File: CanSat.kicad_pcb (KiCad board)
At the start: 2 copper layers, 55.6 x 55.5 mm, 78 parts, among them IC1 W25Q128JVPIQ, J1 USB_C_Receptacle, J2 Conn_Coaxial, M1 SG-90, M2 MountingHole_2.2mm_M2, SW1 SW_Push, SW2 SW_Push, U1 MPU-6050, U4 RFM98W-433S2, U5 RP2350_60QFN, U6 LM1085-5.0, U7 LM1085-3.3, U8 BMP280, U9 APS6404L-3SQR-ZR, Y2 ASE-12.000MHz-E-T

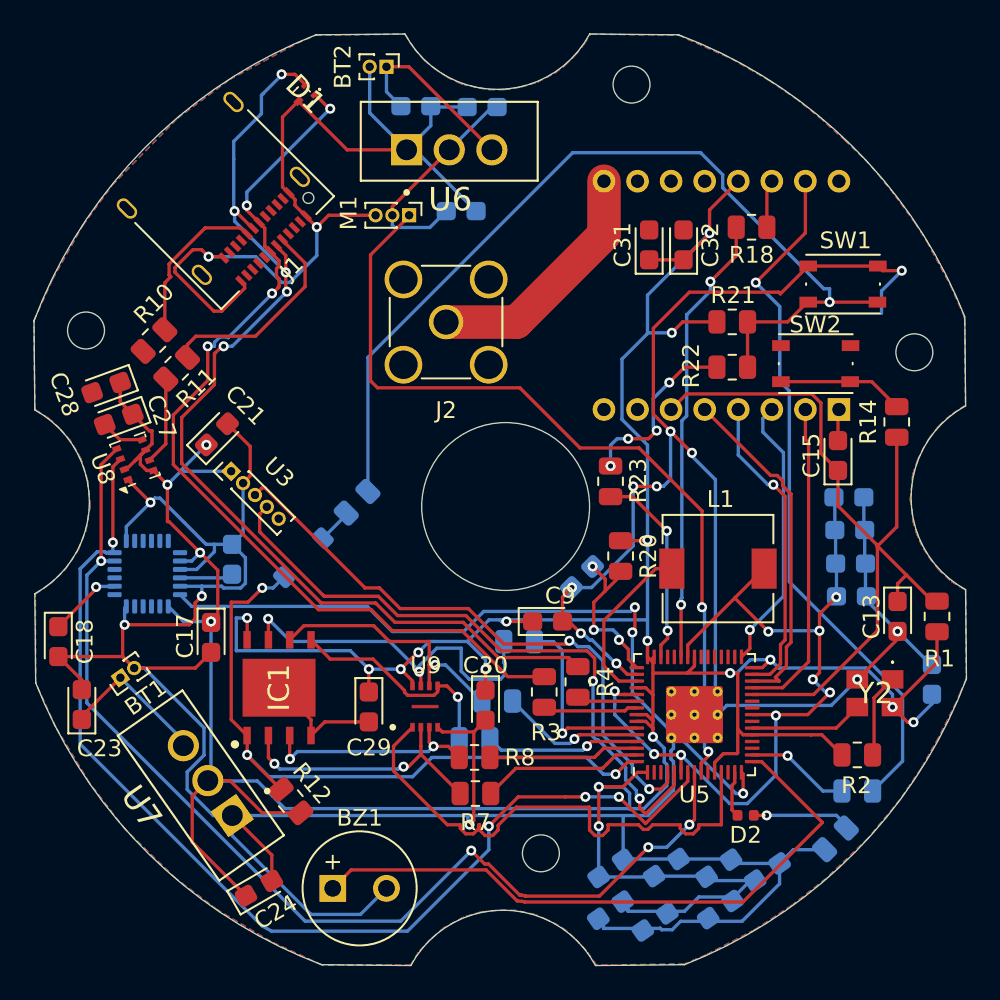
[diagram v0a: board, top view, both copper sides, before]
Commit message: Added pin headers, debug headers, changed power source
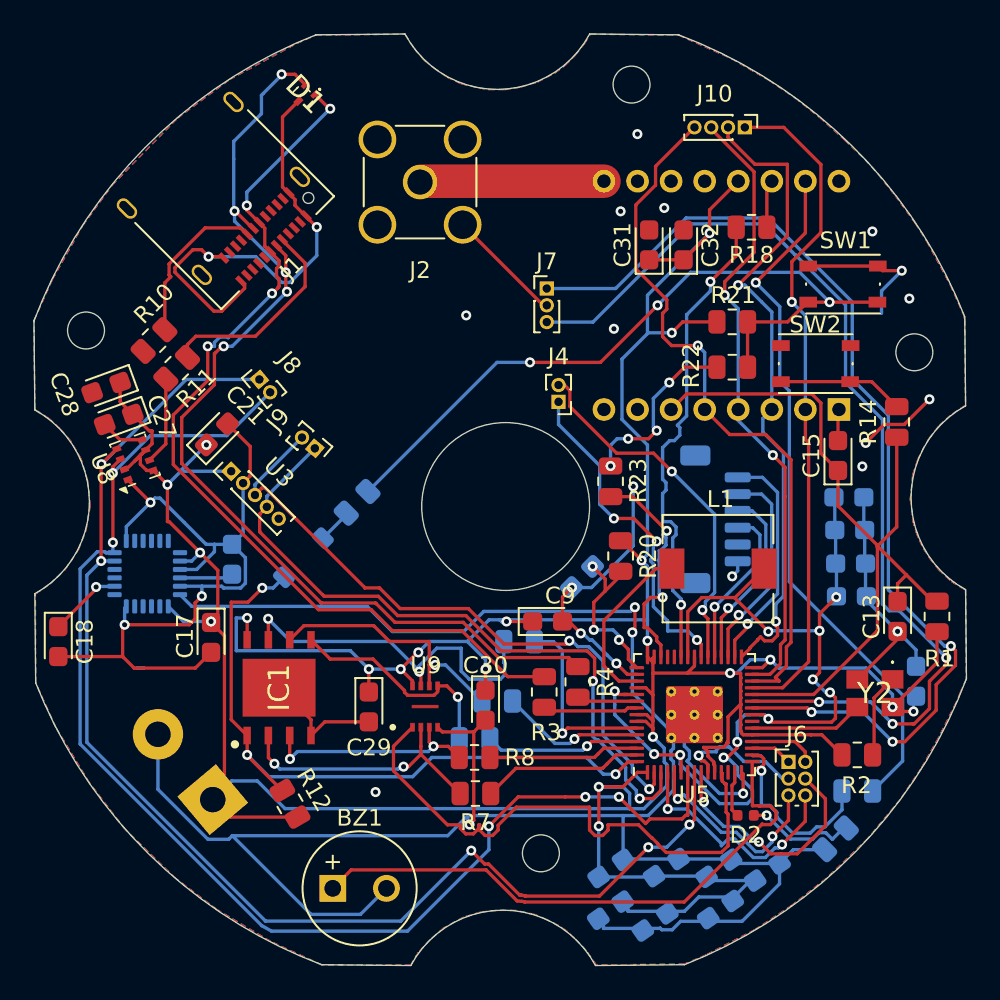
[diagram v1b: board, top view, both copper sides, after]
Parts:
- removed BT1, BT2: Battery, Connector_PinHeader_1.00mm:PinHeader_1x02_P1.00mm_Vertical
- removed C20: 1uF, Capacitor_Tantalum_SMD:CP_EIA-2012-15_AVX-P
- removed C23, C25: 10µf, Capacitor_Tantalum_SMD:CP_EIA-2012-15_AVX-P
- removed C24, C26: 10uf, Capacitor_Tantalum_SMD:CP_EIA-2012-15_AVX-P
- removed M1: SG-90, Connector_PinHeader_1.00mm:PinHeader_1x03_P1.00mm_Vertical
- removed U6: LM1085-5.0, LM1085IT-5.0:TO254P1054X470X1955-3
- removed U7: LM1085-3.3, LM1085IT-3.3:TO254P1054X470X1955-3
- added J10: Conn_01x04_Pin, Connector_PinHeader_1.00mm:PinHeader_1x04_P1.00mm_Vertical, F.Cu at (118.8, 43.4)
- added J3: Conn_01x06_Socket, Connector_JST:JST_SH_BM06B-SRSS-TB_1x06-1MP_P1.00mm_Vertical, B.Cu at (117.0, 66.8)
- added J4: Conn_01x02_Pin, Connector_PinHeader_1.00mm:PinHeader_1x02_P1.00mm_Vertical, F.Cu at (107.7, 59.8)
- added J5: Screw_Terminal_01x02, TerminalBlock:TerminalBlock_bornier-2_P5.08mm, B.Cu at (87.1, 83.5)
- added J6: Conn_01x06_Pin, Connector_PinHeader_1.00mm:PinHeader_2x03_P1.00mm_Vertical, F.Cu at (121.4, 81.2)
- added J7: Conn_01x03_Pin, Connector_PinHeader_1.00mm:PinHeader_1x03_P1.00mm_Vertical, F.Cu at (107.0, 53.0)
- added J8: Conn_01x02_Pin, Connector_PinHeader_1.00mm:PinHeader_1x02_P1.00mm_Vertical, F.Cu at (89.9, 58.4)
- added J9: Conn_01x02_Pin, Connector_PinHeader_1.00mm:PinHeader_1x02_P1.00mm_Vertical, F.Cu at (93.2, 62.5)
- moved J2 8.48 mm to (99.5, 46.7)
- moved C14 0.96 mm to (129.0, 76.4)
- moved R12 0.17 mm to (91.7, 83.7), turned to -60 degrees
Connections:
- net /M1 renamed /RP2350A/GPIO9
- U5 pad 10: /M0 -> /GPIO7
- U5 pad 18: /RP2350A/GPIO14 -> /GPIO14
- U5 pad 19: /RP2350A/GPIO15 -> /GPIO15
- U5 pad 2: /TXD -> /GPS_TX
- U5 pad 24: /RP2350A/SWCLK -> /SWDCLK
- U5 pad 25: /RP2350A/SWDIO -> /SWDIO
- U5 pad 3: /RXD -> /GPS_RX
- U5 pad 32: /RP2350A/GPIO20 -> /DSHOT_1
- U5 pad 33: /RP2350A/GPIO21 -> /DSHOT_2
- U5 pad 34: /RP2350A/GPIO22 -> /DSHOT_3
- U5 pad 35: /RP2350A/GPIO23 -> /DSHOT_4
- U5 pad 36: /RP2350A/GPIO24 -> /PYRO1
- U5 pad 37: /RP2350A/GPIO25 -> /PYRO2
- U5 pad 4: /GPS_TX -> /GPIO2
- U5 pad 5: /GPS_RX -> /GPIO3
- U5 pad 9: /SERVO -> /GPIO6
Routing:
- net GND: track 314.7 -> 239.1 mm, vias 16 -> 24
- net /SWDCLK: track 0.00 -> 62.2 mm, vias 0 -> 3
- net /SWDIO: track 0.00 -> 61.0 mm, vias 0 -> 3
- net /SERVO: track 49.9 -> 0.00 mm, vias 2 -> 0
- net /SPI0_TX: track 16.5 -> 39.1 mm, vias 1 -> 2
- net /SPI0_CSn: track 20.6 -> 42.7 mm, vias 0 -> 1
- net /PYRO1: track 0.00 -> 22.0 mm, vias 0 -> 2
- net /SPI0_RX: track 19.1 -> 40.2 mm, vias 0 -> 1
- net /PYRO2: track 0.00 -> 20.4 mm, vias 0 -> 3
- net /SPI0_SCK: track 18.6 -> 37.3 mm, vias 1 -> 2
- net /GPIO6: track 0.00 -> 14.5 mm, vias 0 -> 2
- net /GPIO2: track 0.00 -> 14.4 mm, vias 0 -> 2
- net /DSHOT_1: track 0.00 -> 13.6 mm, vias 0 -> 1
- net +5V: track 13.5 -> 0.00 mm
- net /I2C0_SCL: track 65.8 -> 78.7 mm, vias 4 -> 5
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
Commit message: Changed LoRa footprint + signed the PCB + added a on/off button
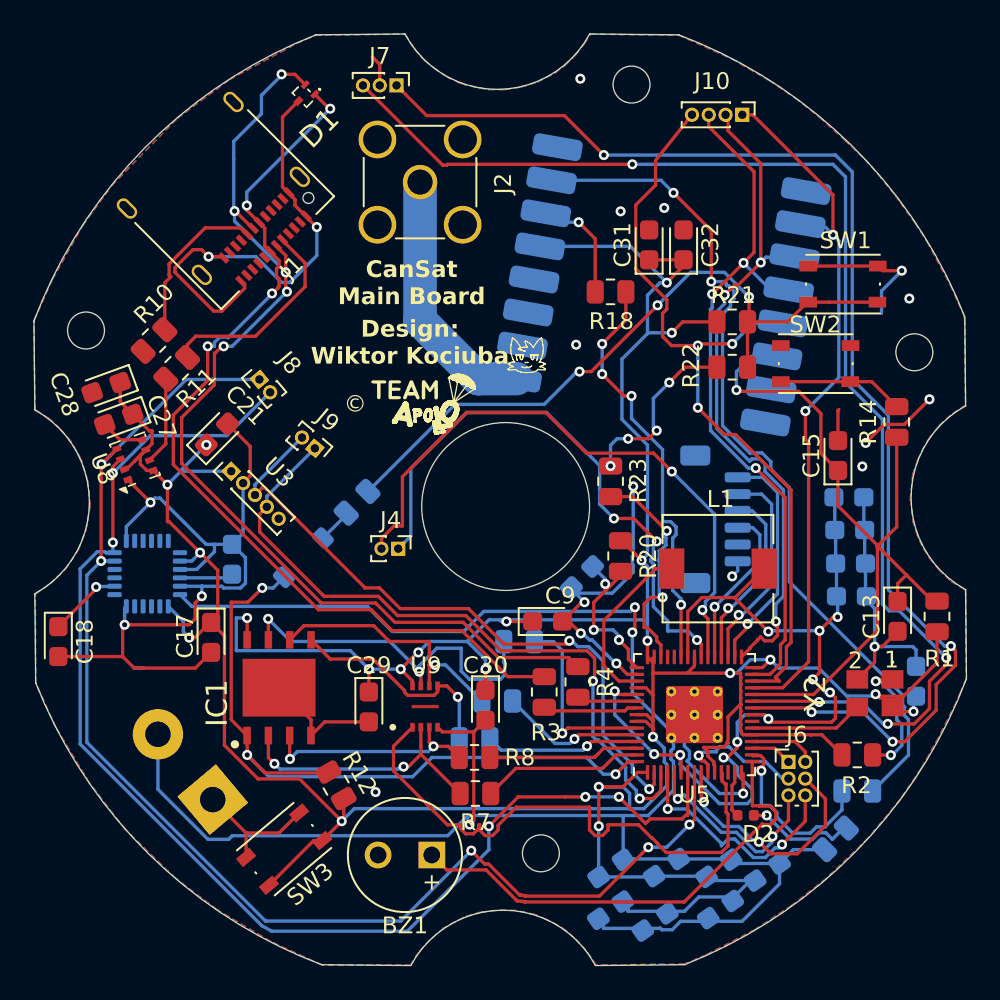
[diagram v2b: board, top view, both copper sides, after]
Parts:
- added SW3: SW_Push, Button_Switch_SMD:SW_Push_1P1T_NO_Vertical_Wuerth_434133025816, F.Cu at (91.3, 86.4)
- D2: value LED -> RED
- U3: value ~ -> Waveshare23721
- U4: footprint RF_Module:HOPERF_RFM9XW_THT -> RF_Module:HOPERF_RFM9XW_SMD
- moved J7 15.1 mm to (98.0, 40.9), turned to -90 degrees
- moved J4 13.0 mm to (98.2, 68.5), turned to -90 degrees
- moved U4 12.9 mm to (113.8, 52.8), turned to 170 degrees
- moved R18 9.24 mm to (110.8, 53.2), turned to 0 degrees
- moved BZ1 6.23 mm to (100.2, 86.8), turned to 180 degrees
- moved R12 2.96 mm to (94.5, 82.6)
- moved J10 0.76 mm to (118.7, 42.6)
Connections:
- J5 pad 1: +3V3 -> Net-(J5-Pin_1)
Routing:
- net /SWDIO: track 61.0 -> 77.5 mm, vias 3 -> 4
- net /SWDCLK: track 62.2 -> 77.2 mm, vias 3 -> 4
- net /PYRO1: track 22.0 -> 36.7 mm
- net /PYRO2: track 20.4 -> 34.6 mm
- net GND: track 239.1 -> 225.7 mm, vias 24 -> 22
- net /RADIO_RX_TIMEOUT: track 41.9 -> 51.5 mm, vias 1 -> 2
- net Net-(J5-Pin_1): track 0.00 -> 7.92 mm
- net /BUZZER: track 34.3 -> 28.3 mm
- net /SPI0_SCK: track 37.3 -> 42.4 mm, vias 2 -> 3
- net Net-(J2-In): track 11.0 -> 15.5 mm
- net Net-(U4-DIO0): track 2.86 -> 6.74 mm, vias 0 -> 1
- net /RADIO_RX_INT: track 28.8 -> 25.0 mm, vias 2 -> 4
- net Net-(R13-Pad1): track 44.6 -> 41.2 mm
- net Net-(Y2-TRI-STATE_(STBY)): track 4.99 -> 7.79 mm, vias 0 -> 2
- net /SPI0_RX: track 40.2 -> 42.8 mm, vias 1 -> 2
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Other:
- board text added: "1"
- board text added: "2"
- board text added: "CanSat Main Board"
- board text added: "Design: Wiktor Kociuba"
- board text added: "©"

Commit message: Fixed design flaw with with components that MCU depends on
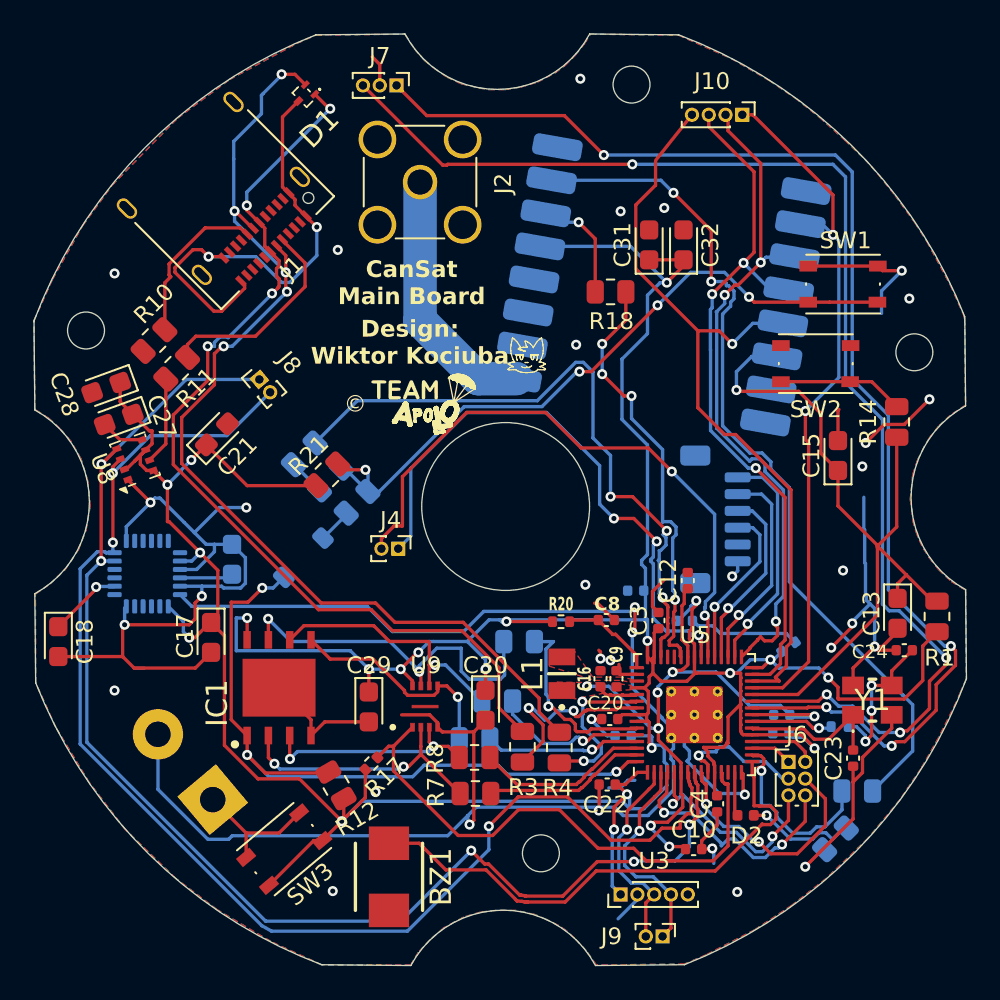
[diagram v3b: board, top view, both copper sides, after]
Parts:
- removed C14: 1uF, Capacitor_Tantalum_SMD:CP_EIA-2012-15_AVX-P
- removed R2: 10K, Resistor_SMD:R_0805_2012Metric
- removed Y2: ASE-12.000MHz-E-T, SamacSys_Parts:ASE12000MHzET
- added C20: 100nF, Capacitor_SMD:C_0402_1005Metric, F.Cu at (110.8, 78.7)
- added C22: 100nF, Capacitor_SMD:C_0402_1005Metric, F.Cu at (110.6, 82.5)
- added C23: 15pF, Capacitor_SMD:C_0402_1005Metric, F.Cu at (125.2, 81.0)
- added C24: 15pF, Capacitor_SMD:C_0402_1005Metric, F.Cu at (128.3, 74.5)
- added R17: 10K, Resistor_SMD:R_0402_1005Metric, F.Cu at (96.5, 81.3)
- added R19: 1K, Resistor_SMD:R_0402_1005Metric, B.Cu at (124.5, 79.1)
- added Y1: Crystal_GND24, clock:ABM8272T3, F.Cu at (126.4, 77.5)
- BZ1: footprint Buzzer_Beeper:MagneticBuzzer_Kingstate_KCG0601 -> buzzer:CMT-4023S
- C1, C11, C2, C5, C6, C7, C9: footprint Capacitor_Tantalum_SMD:CP_EIA-2012-15_AVX-P -> Capacitor_SMD:C_0402_1005Metric
- C10, C12, C16, C3, C4, C8: footprint Capacitor_Tantalum_SMD:CP_EIA-2012-15_AVX-P -> Capacitor_SMD:C_0402_1005Metric; moved to F.Cu
- L1: footprint Inductor_SMD:L_6.3x6.3_H3 -> inductors:AOTAB201610S3R3101T
- R20: footprint Resistor_SMD:R_0805_2012Metric -> Resistor_SMD:R_0402_1005Metric
- R22, R23: moved to B.Cu
- moved J9 35.7 mm to (113.9, 91.6), turned to -90 degrees
- moved U3 34.3 mm to (111.4, 89.1), turned to 90 degrees
- moved R21 25.8 mm to (93.9, 64.1), turned to -135 degrees
- moved R22 24.9 mm to (94.1, 64.3), turned to -135 degrees
- moved C10 21.2 mm to (115.8, 86.4)
- moved C2 19.8 mm to (112.3, 71.0), turned to 180 degrees
- moved C16 18.3 mm to (110.2, 76.2), turned to 90 degrees
- moved R23 18.3 mm to (92.5, 62.9), turned to -135 degrees
- moved C3 17.6 mm to (113.7, 72.8), turned to 90 degrees
- moved C7 15.8 mm to (115.2, 72.8), turned to 0 degrees
- moved C6 13.8 mm to (121.4, 74.3)
- moved L1 11.2 mm to (107.9, 76.0), turned to 90 degrees
- moved C5 10.5 mm to (121.0, 79.5), turned to 180 degrees
- moved C1 10.4 mm to (111.5, 79.7), turned to 180 degrees
- moved C11 9.90 mm to (121.0, 78.4), turned to 180 degrees
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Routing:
- net /GPS_RX: track 41.7 -> 12.6 mm, vias 2 -> 1
- net /GPS_TX: track 39.8 -> 12.1 mm, vias 2 -> 1
- net /USER_SW: track 13.7 -> 39.3 mm, vias 2 -> 3
- net +1V1: track 57.1 -> 41.1 mm, vias 11 -> 7
- net Net-(U5-VREG_LX): track 10.4 -> 0.00 mm
- net GND: track 225.7 -> 216.6 mm, vias 22 -> 34
- net Net-(C24-Pad2): track 0.00 -> 8.89 mm, vias 0 -> 3
- net Net-(R22-Pad2): track 11.0 -> 2.17 mm, vias 4 -> 0
- net Net-(Y2-TRI-STATE_(STBY)): track 7.79 -> 0.00 mm, vias 2 -> 0
- net +3V3: track 243.6 -> 237.1 mm, vias 22 -> 21
- net /RP2350A/N_USB_D+: track 3.61 -> 9.59 mm, vias 0 -> 2
- net /RP2350A/N_USB_D-: track 5.67 -> 11.6 mm, vias 0 -> 2
- net /RP2350A/XOUT: track 0.00 -> 4.91 mm, vias 0 -> 1
- net /RP2350A/VREG_AVDD: track 9.94 -> 5.65 mm, vias 3 -> 0
- net /BUZZER: track 28.3 -> 31.1 mm
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- added copper zone on F.Cu, net +1V1
- added copper zone on F.Cu, net +3V3
- added copper zone on F.Cu, net Net-(U5-VREG_LX)
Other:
- board text removed: "1"
- board text removed: "2"

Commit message: Changed connectors
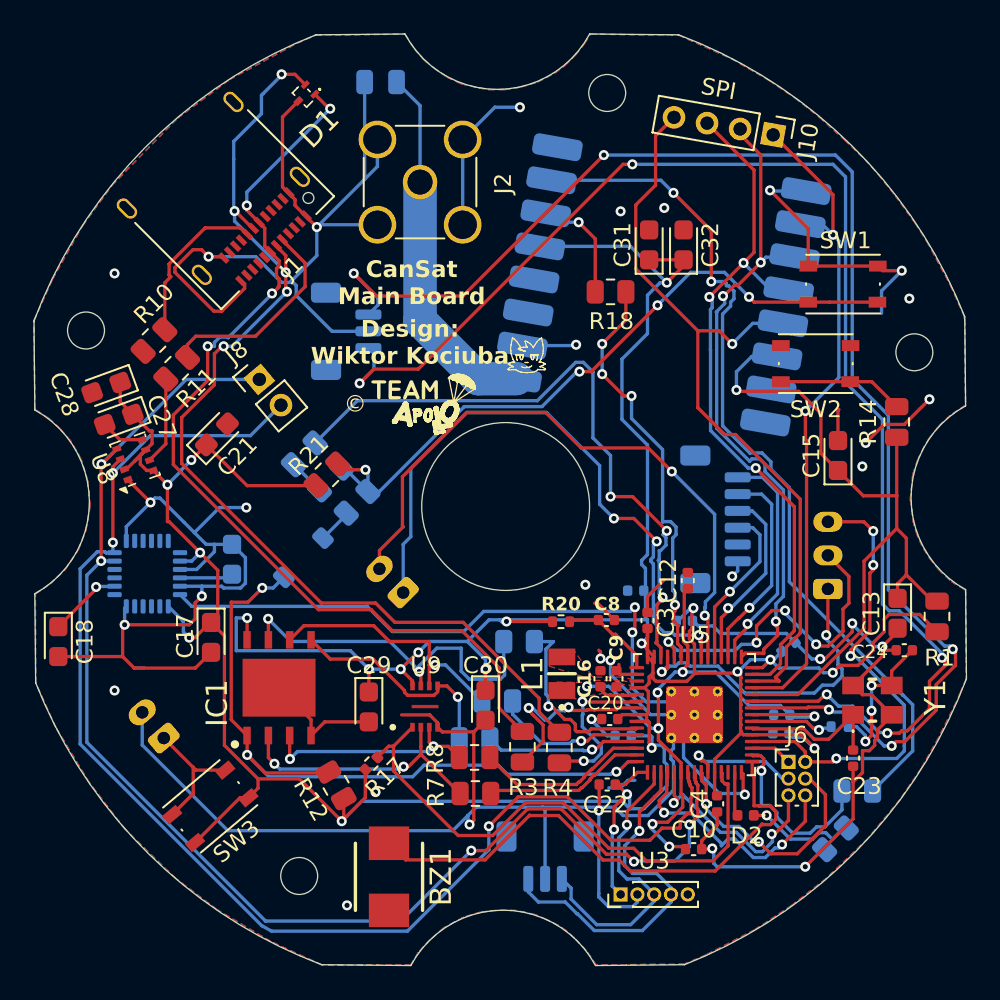
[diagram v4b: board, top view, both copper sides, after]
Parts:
- added C14: DNP, Capacitor_SMD:C_0805_2012Metric, B.Cu at (97.1, 40.7)
- added J11: Conn_01x03_Socket, Connector_JST:JST_PH_B3B-PH-K_1x03_P2.00mm_Vertical, B.Cu at (123.8, 70.9)
- C15, C32: value 100n -> 100nF
- C17: value 0.1uF -> 100nF
- J10: footprint Connector_PinHeader_1.00mm:PinHeader_1x04_P1.00mm_Vertical -> Connector_PinHeader_2.00mm:PinHeader_1x04_P2.00mm_Vertical
- J4: footprint Connector_PinHeader_1.00mm:PinHeader_1x02_P1.00mm_Vertical -> Connector_JST:JST_PH_B2B-PH-K_1x02_P2.00mm_Vertical; moved to B.Cu
- J5: footprint TerminalBlock:TerminalBlock_bornier-2_P5.08mm -> Connector_JST:JST_PH_B2B-PH-K_1x02_P2.00mm_Vertical
- J7: footprint Connector_PinHeader_1.00mm:PinHeader_1x03_P1.00mm_Vertical -> Connector_JST:JST_SH_BM03B-SRSS-TB_1x03-1MP_P1.00mm_Vertical; moved to B.Cu
- J8: footprint Connector_PinHeader_1.00mm:PinHeader_1x02_P1.00mm_Vertical -> Connector_PinHeader_2.00mm:PinHeader_1x02_P2.00mm_Vertical
- J9: footprint Connector_PinHeader_1.00mm:PinHeader_1x02_P1.00mm_Vertical -> Connector_JST:JST_SH_BM03B-SRSS-TB_1x03-1MP_P1.00mm_Vertical; moved to B.Cu
- moved J7 15.0 mm to (95.0, 55.5)
- moved M2 14.5 mm to (92.2, 88.0)
- moved J9 8.46 mm to (106.9, 86.8), turned to 180 degrees
- moved SW3 5.09 mm to (87.0, 83.8)
- moved J5 4.68 mm to (84.2, 79.8)
- moved J4 2.63 mm to (98.4, 71.1), turned to 135 degrees
- moved J10 2.19 mm to (120.5, 43.8), turned to -100 degrees
- moved REF** 1.53 mm to (110.6, 41.4)
- moved C3 0.65 mm to (113.0, 72.8)
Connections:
- net /GPIO15 renamed /BAT_SWITCH
- J9 pad 1: /GPS_RX -> /GPS_TX
- J9 pad 2: /GPS_TX -> GND
- U5 pad 41: /RP2350A/GPIO27/ADC1 -> /PROBE_BAT_1
- U5 pad 42: /RP2350A/GPIO28/ADC2 -> /PROBE_BAT_2
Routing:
- net GND: track 216.6 -> 276.4 mm, vias 34 -> 32
- net /BAT_SWITCH: track 4.02 -> 28.3 mm, vias 0 -> 4
- net /PROBE_BAT_1: track 0.00 -> 19.8 mm, vias 0 -> 4
- net /PROBE_BAT_2: track 0.00 -> 19.2 mm, vias 0 -> 2
- net /GPS_RX: track 12.6 -> 21.9 mm
- net /SWDCLK: track 77.4 -> 85.6 mm, vias 4 -> 5
- net Net-(J2-In): track 15.5 -> 22.0 mm
- net /SWDIO: track 78.2 -> 84.5 mm, vias 4 -> 5
- net +3V3: track 237.1 -> 231.7 mm
- net /GPS_TX: track 12.1 -> 17.4 mm
- net /SPI0_CSn: track 43.7 -> 47.2 mm
- net /SPI0_RX: track 42.8 -> 40.1 mm
- net /PYRO2: track 34.9 -> 37.5 mm
- net /SPI0_TX: track 40.7 -> 39.5 mm
- net /PYRO1: track 36.6 -> 37.6 mm
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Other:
- board text added: "BAT PROBE"
- board text added: "DSHOT"
- board text added: "GP"
- board text added: "GPS"
- board text added: "I2C"
- board text added: "PICO PROBE"
- board text added: "PWR"
- board text added: "PYRO"
- board text added: "SPI"
- board text added: "UART DEBUG"

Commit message: Readme Update
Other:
- board text added: "404 Not Found"
- board text added: ":3"
- board text added: "I like to move it move it"
- board text added: "Lima Oscar Romeo Alpha"
- board text added: "Romeo Foxtrot Mike Niner Eight Whisky"
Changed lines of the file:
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@@
 	(title_block
 		(title "Main Board")
-		(date "2026-03-11")
-		(rev "v3.0.0")
+		(date "2026-03-13")
+		(rev "v3.1.0")
 		(company "Team ApolLO")
 		(comment 1 "Author: Wiktor Kociuba")
@@
 			(pdf_back_fp_property_popups yes)
 			(pdf_metadata yes)
-			(pdf_single_document no)
+			(pdf_single_document yes)
 			(dxfpolygonmode yes)
 			(dxfimperialunits yes)
@@
 			(crossoutdnponfab yes)
 			(subtractmaskfromsilk no)
-			(outputformat 5)
+			(outputformat 4)
 			(mirror no)
 			(drillshape 0)
@@
 		)
 	)
+	(gr_text "404 Not Found"
+		(at 118.25 81.25 90)
+		(layer "F.SilkS")
+		(effects
+			(font
+				(size 0.5 0.5)
+				(thickness 0.125)
+				(bold yes)
+			)
+			(justify left bottom)
+		)
+	)
+	(gr_text ":3"
+		(at 86.4 47.25 45)
+		(layer "F.SilkS")
+		(effects
+			(font
+				(size 1 1)
+				(thickness 0.15)
+			)
+			(justify left bottom)
+		)
+	)
 	(gr_text "SPI"
 		(at 116.1 41.5 350)
@@
 		)
 	)
+	(gr_text "Romeo\nFoxtrot\nMike\nNiner\nEight\nWhisky\n"
+		(at 114.95 47.85 170)
+		(layer "B.SilkS")
+		(effects
+			(font
+				(size 1 1)
+				(thickness 0.15)
+			)
+			(justify left bottom mirror)
+		)
+	)
 	(gr_text "PYRO"
 		(at 98.8 74.5 225)
@@
 		(layer "B.SilkS")
 		(effects
+			(font
+				(size 1 1)
+				(thickness 0.15)
+			)
+			(justify left bottom mirror)
+		)
+	)
+	(gr_text "I like to \nmove it \nmove it"
+		(at 82.4 69.9 270)
+		(layer "B.SilkS")
+		(effects
+			(font
+				(size 0.4 0.4)
+				(thickness 0.1)
+				(bold yes)
+			)
+			(justify bottom mirror)
+		)
+	)
+	(gr_text "Lima\nOscar\nRomeo\nAlpha"
+		(at 109.2 48.7 170)
+		(layer "B.SilkS")
+		(effects
